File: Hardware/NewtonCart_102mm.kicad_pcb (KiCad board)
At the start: 2 copper layers, 99.7 x 39 mm, 29 parts, among them J3 Reserve IO's, M3 MountingHole_3.2mm_M3, U2 LM1117-3.3

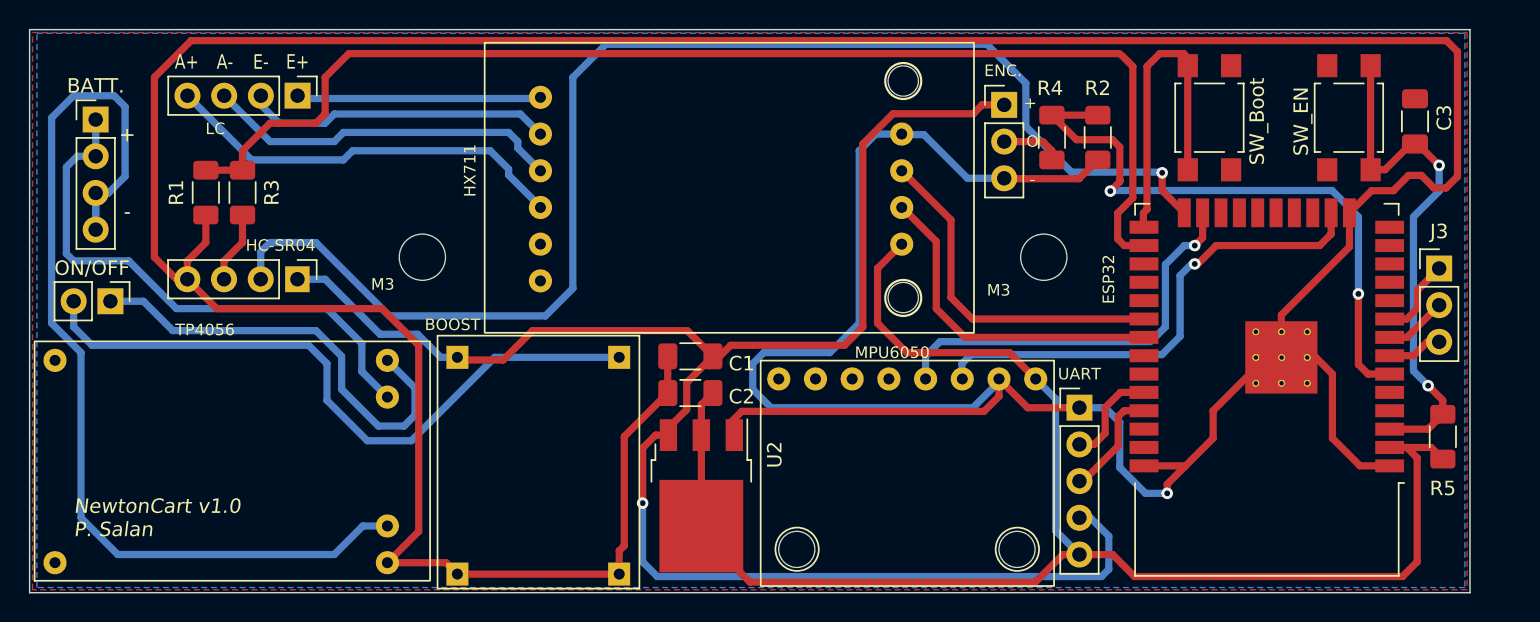
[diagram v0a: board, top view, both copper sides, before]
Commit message: Se añaden versiones creadas de PCB, nuevas modificaciones tanto en PCB como en esquemático. Se añade funcionalidad para Encendido/Apagado de la plataforma, se añade y se modifican botones de "Boot" y "Enable" de acuerdo a documentación para asegurar la funcionalidad UART con el ESP32-WROOM32D montado en la PCB. **archivos NewtonCart.kicad corresponden a archivo final, con el que se envió a realizar PCB.**
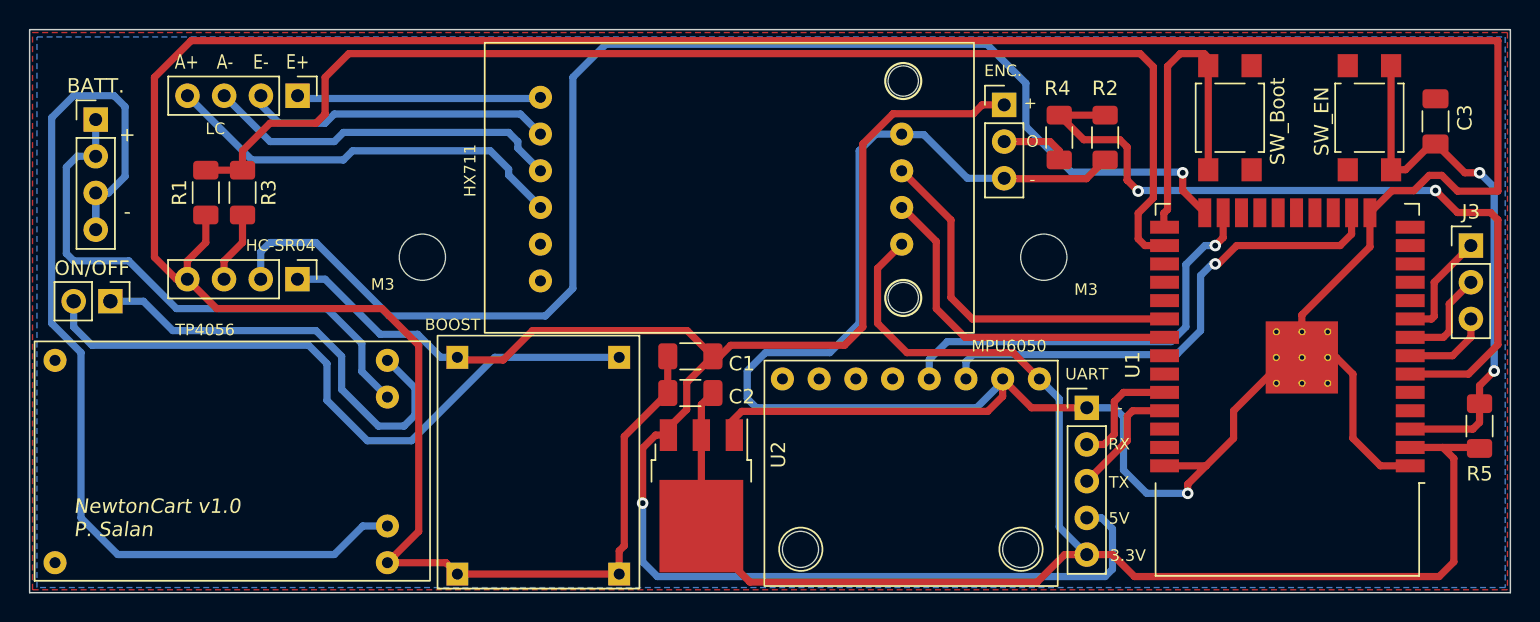
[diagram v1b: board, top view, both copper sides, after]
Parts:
- moved J3 2.71 mm to (152.3, 136.1)
- moved R5 2.64 mm to (152.9, 148.6)
- moved C3 1.42 mm to (149.9, 127.5)
- moved SW_EN 1.42 mm to (145.3, 127.3)
- moved SW_Boot 1.42 mm to (135.6, 127.3)
- moved U1 1.42 mm to (139.6, 143.1)
- moved UART 0.51 mm to (125.7, 147.3)
- moved R4 0.51 mm to (123.8, 128.6)
- moved R2 0.51 mm to (127.0, 128.6)
- moved MPU6050 0.25 mm to (123.7, 144.1)
- moved REF** 0.25 mm to (105.9, 157.1)
- moved REF** 0.25 mm to (121.2, 157.1)
- renumbered ESP32-WROOM32 to U1
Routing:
- net VEL_PULSE: track 42.7 -> 53.5 mm
- net 4056OUT-: track 336.9 -> 345.3 mm
- net 3.3Reg: track 107.0 -> 110.7 mm
- net Net-(J3-Pad2): track 4.34 -> 6.89 mm
- net Net-(J3-Pad3): track 3.82 -> 6.00 mm
- net Net-(J3-Pad1): track 5.61 -> 7.69 mm
- net Net-(C3-Pad1): track 36.0 -> 37.7 mm
- net US_ECHO: track 84.3 -> 85.9 mm
- net LC_SCK: track 23.2 -> 24.6 mm
- net LC_DT: track 24.2 -> 25.6 mm
- net US_TRIGGER: track 91.8 -> 93.2 mm
- net Net-(J4-Pad2): track 7.00 -> 8.20 mm
- net MPU_SDA: track 28.3 -> 29.4 mm
- net MPU_SCL: track 34.3 -> 35.2 mm
- net Net-(J4-Pad3): track 7.68 -> 8.39 mm
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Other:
- board size 99.7 x 39 mm -> 102.5 x 39 mm
- board text removed: "ESP32"
